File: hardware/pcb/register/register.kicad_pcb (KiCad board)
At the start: 2 copper layers, 62.2 x 21.6 mm, 50 parts, among them J1 Conn_01x08_Male, J2 Conn_01x04_Male, J3 Conn_01x04_Male, J4 Conn_01x04_Male, J5 Conn_01x08_Male, J6 Conn_01x08_Male, U1 74HC245, U2 74HC173, U3 74HC173, U4 74HC173, U5 74HC173, U6 74HC245, U7 74HC245

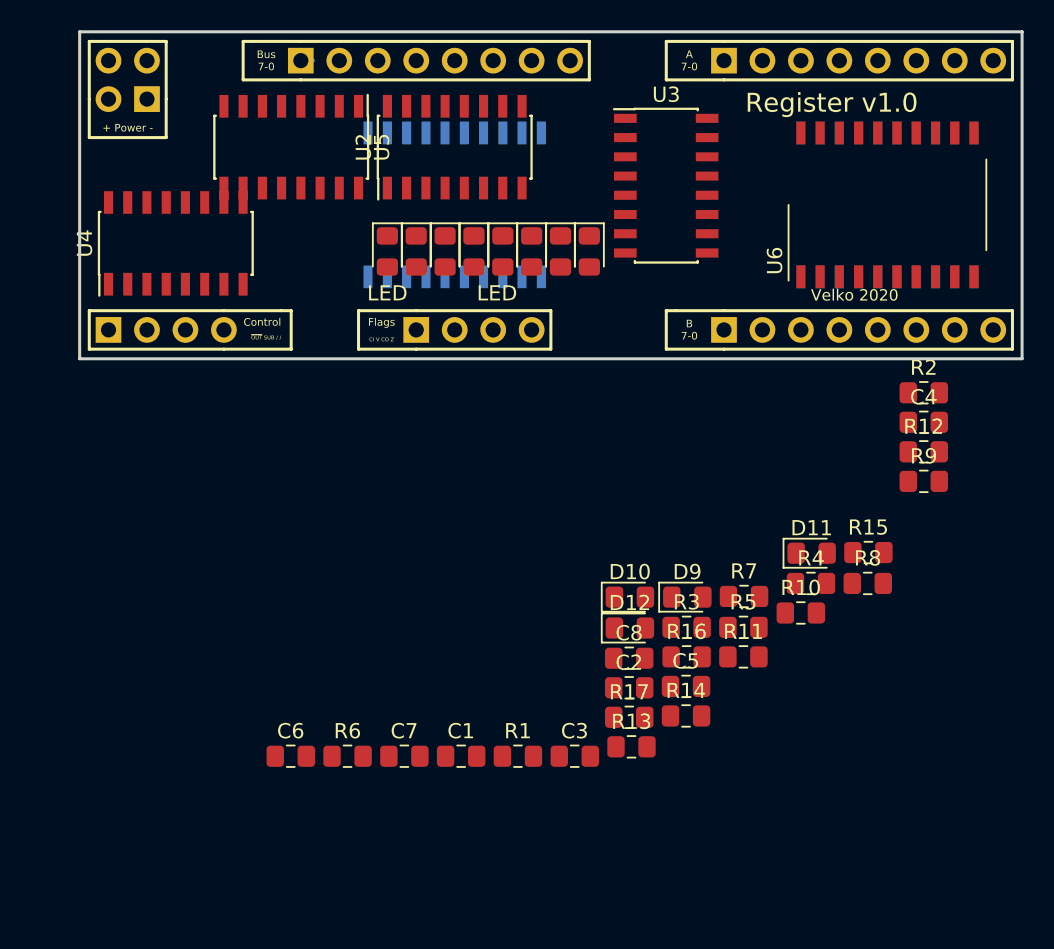
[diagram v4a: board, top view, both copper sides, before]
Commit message: Re-arrange data connections, pre-route
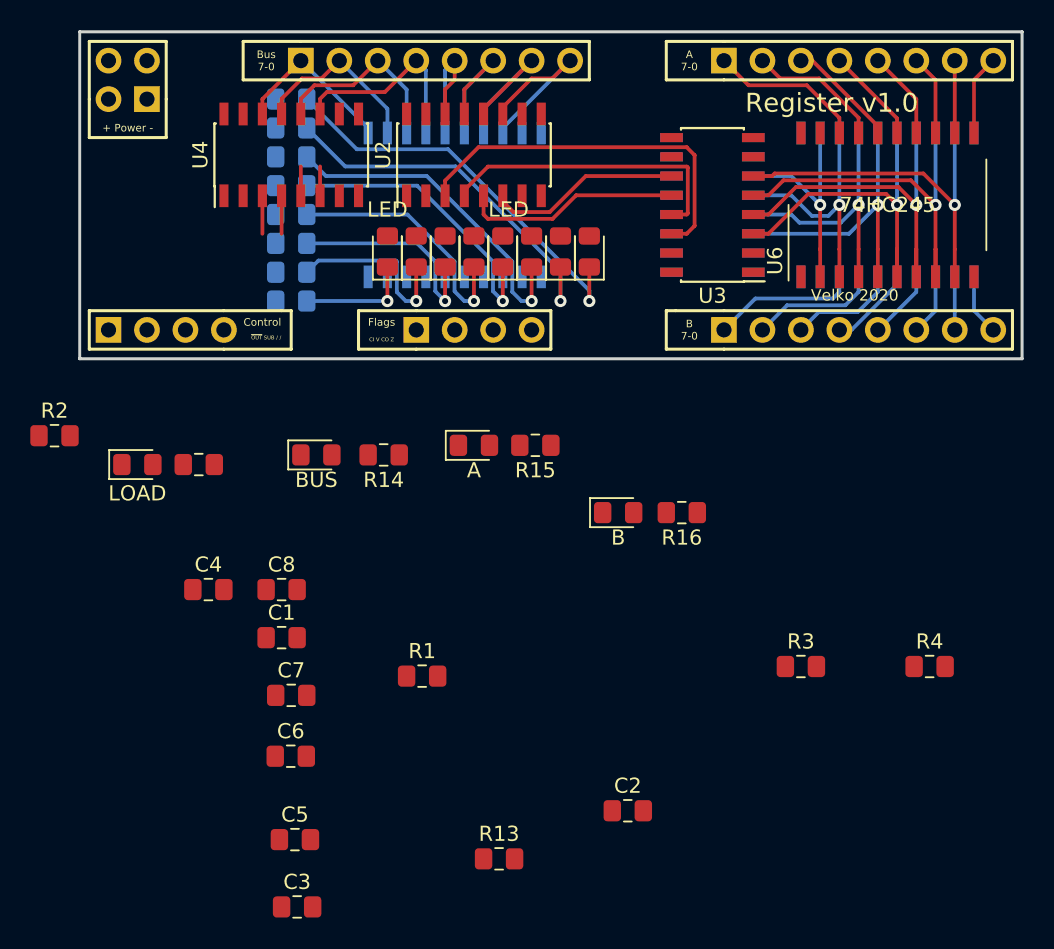
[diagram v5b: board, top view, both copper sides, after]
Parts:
- D10: value LED -> BUS
- D11: value LED -> A
- D12: value LED -> B
- D9: value LED -> LOAD
- R10, R11, R12, R5, R6, R7, R8, R9, U5: moved to B.Cu
- moved R2 57.5 mm to (33.3, 62.9)
- moved C4 48.5 mm to (43.4, 73.0)
- moved R8 46.3 mm to (48.9, 46.4)
- moved R5 45.9 mm to (48.9, 40.6)
- moved R9 45.3 mm to (48.9, 48.3)
- moved R12 42.9 mm to (48.9, 54.0)
- moved R7 41.7 mm to (48.9, 44.5)
- moved R6 41.7 mm to (48.9, 42.5)
- moved R10 41.6 mm to (48.9, 50.2)
- moved R11 39.2 mm to (48.9, 52.1)
- moved D9 37.4 mm to (38.7, 64.8)
- moved R17 33.0 mm to (42.8, 64.8)
- moved U5 28.1 mm to (76.7, 47.6), turned to 180 degrees
- moved C5 27.7 mm to (49.1, 89.5)
- moved R14 26.4 mm to (55.0, 64.1), turned to 180 degrees
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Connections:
- U1 pad 11: BUS0 -> BUS7
- U1 pad 12: BUS1 -> BUS6
- U1 pad 13: BUS2 -> BUS5
- U1 pad 14: BUS3 -> BUS4
- U1 pad 15: BUS4 -> BUS3
- U1 pad 16: BUS5 -> BUS2
- U1 pad 17: BUS6 -> BUS1
- U1 pad 18: BUS7 -> BUS0
- U1 pad 2: TAP7 -> TAP0
- U1 pad 3: TAP6 -> TAP1
- U1 pad 4: TAP5 -> TAP2
- U1 pad 5: TAP4 -> TAP3
- U1 pad 6: TAP3 -> TAP4
- U1 pad 7: TAP2 -> TAP5
- U1 pad 8: TAP1 -> TAP6
- U1 pad 9: TAP0 -> TAP7
- U2 pad 11: BUS3 -> BUS0
- U2 pad 12: BUS2 -> BUS1
- U2 pad 13: BUS1 -> BUS2
- U2 pad 14: BUS0 -> BUS3
- U2 pad 3: M0 -> M3
- U2 pad 4: M1 -> M2
- U2 pad 5: M2 -> M1
- U2 pad 6: M3 -> M0
- U3 pad 10: LOAD -> GND
- U3 pad 11: M3 -> M0
- U3 pad 12: M2 -> M1
- U3 pad 13: M1 -> M2
- U3 pad 14: M0 -> M3
- U3 pad 3: TAP0 -> TAP3
- U3 pad 4: TAP1 -> TAP2
- U3 pad 5: TAP2 -> TAP1
- U3 pad 6: TAP3 -> TAP0
- U3 pad 9: LOAD -> GND
- U4 pad 11: BUS7 -> BUS4
- U4 pad 12: BUS6 -> BUS5
- U4 pad 13: BUS5 -> BUS6
- U4 pad 14: BUS4 -> BUS7
- U4 pad 3: M4 -> M7
- U4 pad 4: M5 -> M6
- U4 pad 5: M6 -> M5
- U4 pad 6: M7 -> M4
- U5 pad 10: LOAD -> GND
- U5 pad 11: M7 -> M4
- U5 pad 12: M6 -> M5
- U5 pad 13: M5 -> M6
- U5 pad 14: M4 -> M7
- U5 pad 3: TAP4 -> TAP7
- U5 pad 4: TAP5 -> TAP6
- U5 pad 5: TAP6 -> TAP5
- U5 pad 6: TAP7 -> TAP4
- U5 pad 9: LOAD -> GND
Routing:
- net Net-(D1-Pad1): track 0.00 -> 26.8 mm, vias 0 -> 1
- net Net-(D2-Pad1): track 0.00 -> 25.2 mm, vias 0 -> 1
- net M3: track 0.00 -> 25.1 mm
- net TAP1: track 0.00 -> 24.8 mm, vias 0 -> 1
- net TAP0: track 0.00 -> 23.7 mm, vias 0 -> 1
- net TAP2: track 0.00 -> 23.7 mm, vias 0 -> 1
- net TAP3: track 0.00 -> 22.6 mm, vias 0 -> 1
- net Net-(D3-Pad1): track 0.00 -> 22.5 mm, vias 0 -> 1
- net M2: track 0.24 -> 19.9 mm
- net Net-(D4-Pad1): track 0.10 -> 19.5 mm, vias 0 -> 1
- net TAP4: track 0.00 -> 18.5 mm, vias 0 -> 1
- net TAP5: track 0.00 -> 17.5 mm, vias 0 -> 1
- net Net-(D5-Pad1): track 0.00 -> 16.8 mm, vias 0 -> 1
- net TAP6: track 0.00 -> 16.0 mm, vias 0 -> 1
- net TAP7: track 0.00 -> 14.7 mm, vias 0 -> 1
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
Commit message: Place all the components
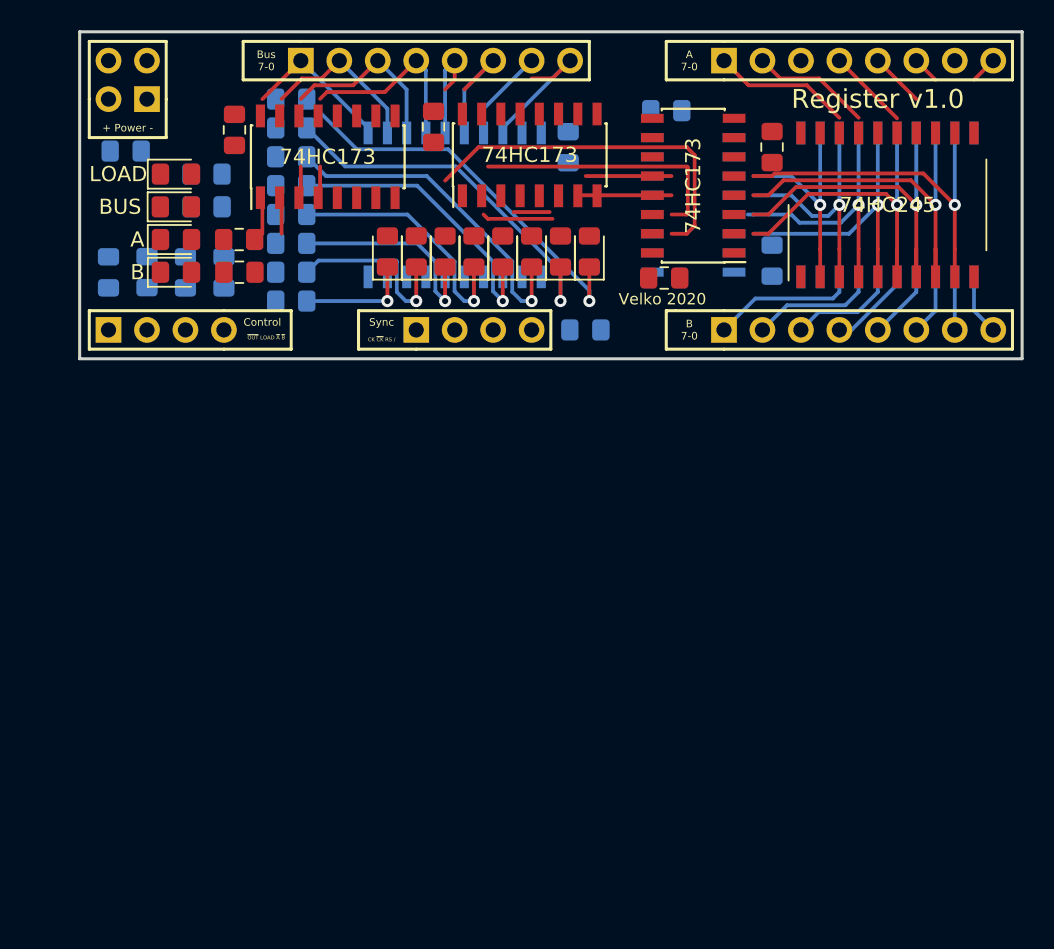
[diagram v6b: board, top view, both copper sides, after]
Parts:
- C1, C2, C5, C7, R1, R13, R14, R17, R2, R3, R4: moved to B.Cu
- moved C2 54.7 mm to (38.0, 44.1)
- moved C5 54.0 mm to (73.7, 41.4)
- moved R4 53.4 mm to (44.5, 52.1), turned to 270 degrees
- moved C6 51.3 mm to (80.6, 43.8), turned to 270 degrees
- moved R3 50.4 mm to (39.4, 52.1), turned to 270 degrees
- moved C3 48.1 mm to (73.5, 52.5)
- moved C1 40.8 mm to (80.6, 51.3), turned to 90 degrees
- moved C7 40.6 mm to (67.2, 43.8), turned to 90 degrees
- moved R13 35.4 mm to (68.3, 55.9), turned to 180 degrees
- moved R1 33.8 mm to (36.8, 52.1), turned to 270 degrees
- moved R16 33.2 mm to (45.5, 52.1)
- moved D12 33.2 mm to (41.3, 52.1)
- moved C8 32.2 mm to (58.3, 42.5), turned to 270 degrees
- moved C4 30.4 mm to (45.1, 42.7), turned to 270 degrees
- moved D11 23.9 mm to (41.3, 49.9)
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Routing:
- net RESET: track 0.00 -> 24.0 mm
- net M2: track 19.9 -> 0.00 mm
- net M0: track 12.8 -> 2.39 mm
- net M3: track 25.1 -> 17.8 mm
- net A5: track 7.45 -> 1.33 mm
- net BUS1: track 11.3 -> 6.11 mm
- net A1: track 4.77 -> 0.00 mm
- net A2: track 5.30 -> 1.80 mm
- net A0: track 5.30 -> 1.80 mm
- net BUS0: track 12.8 -> 9.65 mm
- net GND: track 0.00 -> 2.87 mm
- net A3: track 5.83 -> 3.59 mm
- net M1: track 14.4 -> 16.6 mm
- net M7: track 2.86 -> 4.80 mm
- net M5: track 1.94 -> 0.00 mm
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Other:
- board text added: "CK ~CK~ RS /"
- board text added: "Sync"
- board text added: "~OUT~ LOAD ~A~ ~B~"
- board text removed: "CI V CO Z"
- board text removed: "Flags"
- board text removed: "~OUT~ SUB / /"

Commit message: Clean up pre-routed tracks
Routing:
- net Net-(D1-Pad1): track 26.8 -> 0.00 mm, vias 1 -> 0
- net Net-(D2-Pad1): track 25.2 -> 0.30 mm, vias 1 -> 0
- net TAP1: track 24.8 -> 0.00 mm, vias 1 -> 0
- net RESET: track 24.0 -> 0.00 mm
- net TAP0: track 23.7 -> 0.00 mm, vias 1 -> 0
- net TAP2: track 23.7 -> 0.00 mm, vias 1 -> 0
- net TAP3: track 22.6 -> 0.00 mm, vias 1 -> 0
- net Net-(D3-Pad1): track 22.5 -> 0.24 mm, vias 1 -> 0
- net Net-(D4-Pad1): track 19.5 -> 0.00 mm, vias 1 -> 0
- net TAP4: track 18.5 -> 0.00 mm, vias 1 -> 0
- net TAP5: track 17.5 -> 0.00 mm, vias 1 -> 0
- net M3: track 17.8 -> 0.47 mm
- net Net-(D5-Pad1): track 16.8 -> 0.00 mm, vias 1 -> 0
- net M1: track 16.6 -> 0.00 mm
- net TAP6: track 16.0 -> 0.00 mm, vias 1 -> 0
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
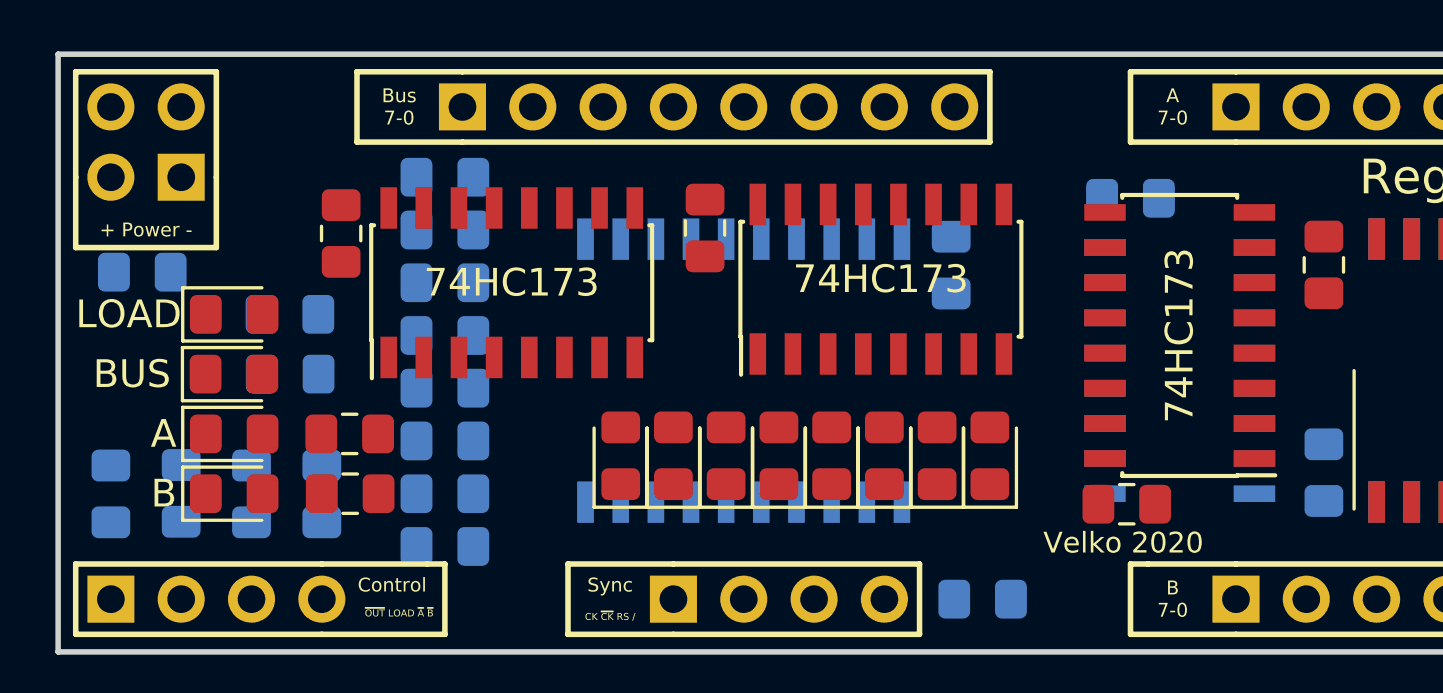
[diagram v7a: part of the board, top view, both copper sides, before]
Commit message: Slight re-arrange (move)
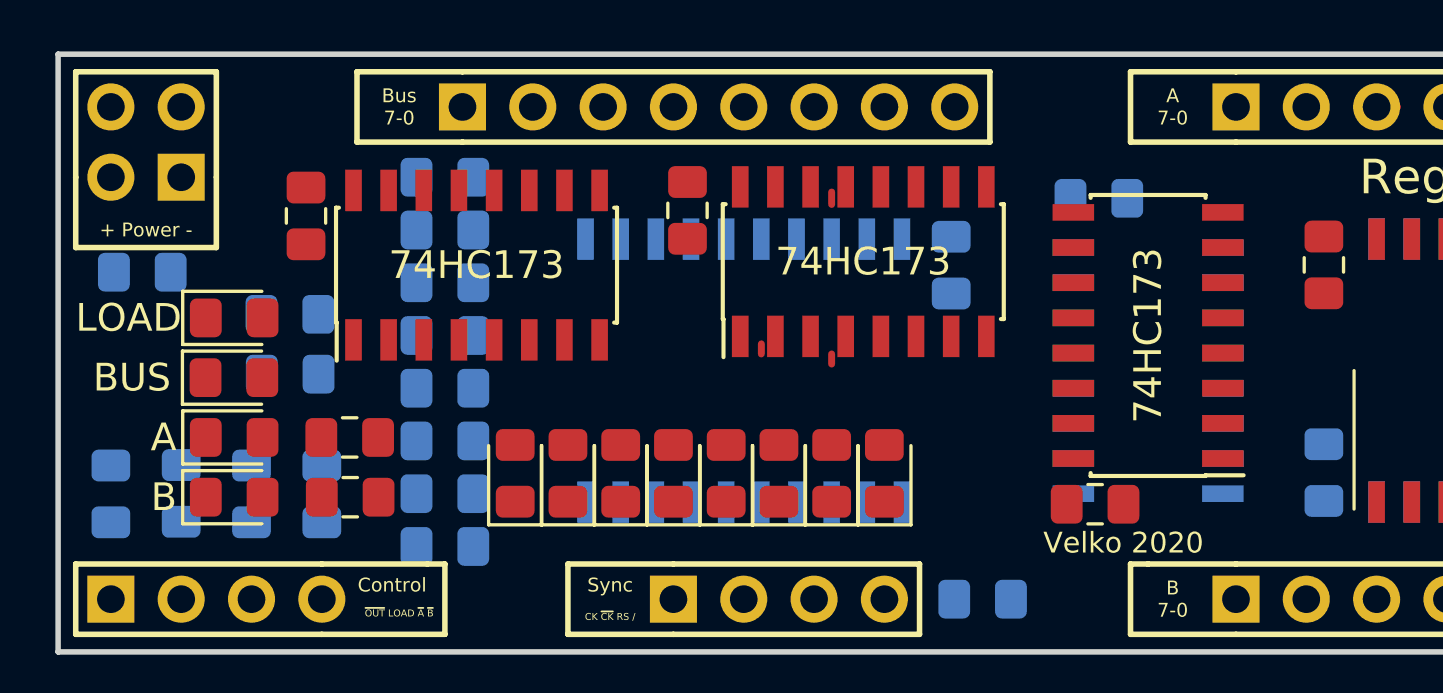
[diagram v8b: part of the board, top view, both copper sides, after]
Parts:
- moved D1 3.86 mm to (64.8, 51.3)
- moved D4 3.86 mm to (59.1, 51.3)
- moved D5 3.86 mm to (57.1, 51.3)
- moved D6 3.86 mm to (55.2, 51.3)
- moved D2 3.86 mm to (62.9, 51.3)
- moved D3 3.86 mm to (61.0, 51.3)
- moved D7 3.86 mm to (53.3, 51.3)
- moved D8 3.86 mm to (51.4, 51.3)
- moved U4 1.42 mm to (50.0, 43.8)
- moved C4 1.42 mm to (43.9, 42.0)
- moved C3 1.14 mm to (72.4, 52.5)
- moved C5 1.14 mm to (72.5, 41.4)
- moved U3 1.14 mm to (74.3, 46.4)
- moved U5 1.14 mm to (74.3, 47.6)
- moved U2 0.90 mm to (64.0, 43.7)
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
